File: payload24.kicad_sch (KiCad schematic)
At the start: 21 parts, among them J1 532540370, J2 532540370, J3 460150206, J4 532540370, Q1 CSD19503KCS, Q2 CSD19503KCS, SW1 FingerTech

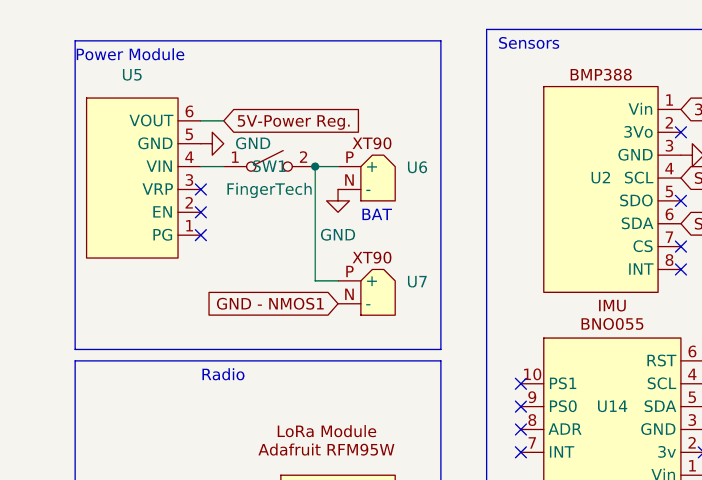
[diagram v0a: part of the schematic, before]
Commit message: PCB layer and power setup
Made PCB 6-Layers
Routed .1in power connection
Setup power plane thermal relief spoke width and gap
Moved Mosfet, power regular, and other components around a little
Rotated PCB 21 degrees
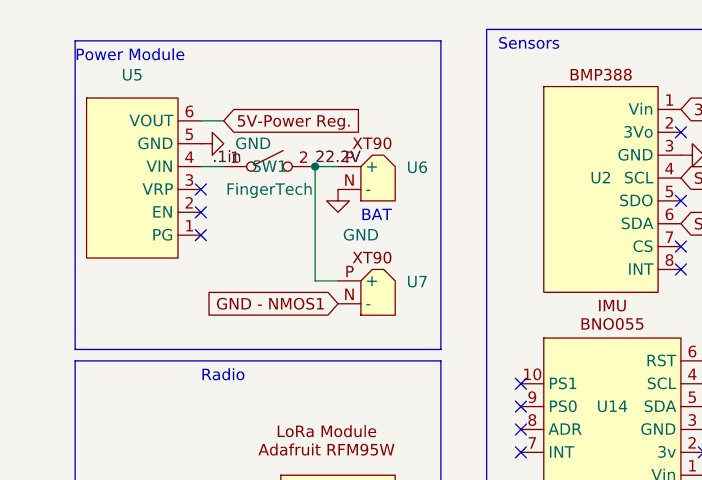
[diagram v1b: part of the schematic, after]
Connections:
- net 22.2V: now reaches SW1.2 (B), U6.P (+), U7.P (+)
- net .1in: now reaches SW1.1 (A), U5.4 (VIN)
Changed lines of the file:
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@@
+    (effects (font (size 1.27 1.27)) (justify left bottom))
+  )
+  (label "22.2V" (at 46.99 30.48 0) (fields_autoplaced)
+    (effects (font (size 1.27 1.27)) (justify left bottom))
+  )
+  (label ".1in" (at 35.56 30.48 0) (fields_autoplaced)
     (effects (font (size 1.27 1.27)) (justify left bottom))
   )
@@
   )
   (symbol (lib_id "power:GND") (at 49.53 33.02 0) (unit 1)
-    (in_bom yes) (on_board yes) (dnp no) (fields_autoplaced)
+    (in_bom yes) (on_board yes) (dnp no)
     (property "Reference" "#PWR018" (at 49.53 39.37 0)
       (effects (font (size 1.27 1.27)) hide)
     )
-    (property "Value" "GND" (at 49.53 38.1 0)
-      (effects (font (size 1.27 1.27)))
-    )
+    (property "Value" "GND" (at 52.07 38.1 0)
+      (effects (font (size 1.27 1.27)))
+    )

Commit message: final updates prior to purchasing (1/17)
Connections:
- net GND: now also Q2.3, R3.1
- net GND - NMOS1: no longer Q2.3, R3.1
- net Altitude Signal: no longer names the net of U1.29 (PWM|TX7)
- no-connect marks 53 -> 54
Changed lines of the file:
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@@
   (no_connect (at 58.42 87.63))
   (no_connect (at 90.17 92.71))
+  (no_connect (at 130.81 72.39))
   (no_connect (at 90.17 85.09))
   (no_connect (at 58.42 74.93))
@@
     )
   )
-  (global_label "GND - NMOS1" (shape input) (at 59.69 124.46 180) (fields_autoplaced)
-    (effects (font (size 1.27 1.27)) (justify right))
-    (property "Intersheetrefs" "${INTERSHEET_REFS}" (at 42.7953 124.46 0)
-      (effects (font (size 1.27 1.27)) (justify right) hide)
-    )
-  )
   (global_label "SCL1" (shape input) (at 87.63 110.49 0) (fields_autoplaced)
     (effects (font (size 1.27 1.27)) (justify left))
@@
     (effects (font (size 1.27 1.27)) (justify right))
     (property "Intersheetrefs" "${INTERSHEET_REFS}" (at 123.2286 54.61 0)
-      (effects (font (size 1.27 1.27)) (justify right) hide)
-    )
-  )
-  (global_label "Altitude Signal" (shape input) (at 130.81 72.39 180) (fields_autoplaced)
-    (effects (font (size 1.27 1.27)) (justify right))
-    (property "Intersheetrefs" "${INTERSHEET_REFS}" (at 113.7341 72.39 0)
       (effects (font (size 1.27 1.27)) (justify right) hide)
     )
@@
         )
       )
+    )
+  )
+  (symbol (lib_id "power:GND") (at 59.69 124.46 0) (unit 1)
+    (in_bom yes) (on_board yes) (dnp no)
+    (property "Reference" "#PWR02" (at 59.69 130.81 0)
+      (effects (font (size 1.27 1.27)) hide)
+    )
+    (property "Value" "GND" (at 59.69 127 90)
+      (effects (font (size 1.27 1.27)) (justify right))
+    )
+    (property "Footprint" "" (at 59.69 124.46 0)
+      (effects (font (size 1.27 1.27)) hide)
+    )
+    (property "Datasheet" "" (at 59.69 124.46 0)
+      (effects (font (size 1.27 1.27)) hide)
+    )
+    (pin "1")
+    (instances
+      (project "payload24"
+        (path "/2e97abcc-083d-4cb7-a03a-25669793abd8"
+          (reference "#PWR02") (unit 1)
+        )
+      )

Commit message: PCB laid out
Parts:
- removed J1, J2, J4: 532540370, JST-XH3:JST-XH3, symbol molexConnector:532540370
- removed J3: 460150206, JST-XH2:JST-XH2, symbol molex2pin:460150206
- removed Q1: CSD19503KCS, teensyMosfet:teensyMosfet, symbol teensyMosfet:CSD19503KCS
- removed R1: 500, 500Ohm:RESC3216X65N, symbol Device:R_US
- removed R4: 10K, 10KOhm:RESC3216X70N, symbol Device:R_US
- removed U13: ~, Trinket M0:Trinket M0, symbol Trinket M0:Trinket_M0
- removed U2: ~, BMP388:BMP388, symbol BMP388:BMP388
- removed U7: ~, XT60:AMASS_XT60-M, symbol PowerConnectors:XT90
- added J1: JST-XH3, JST-XH3:JST-XH3, symbol 532540370:JST-XH3
- added J2: PixHawk, JST-XH2:JST-XH2, symbol 532540370:JST-XH2
- added J3, J4: Motors, JST-XH3:JST-XH4, symbol 532540370:JST-XH4
- added Q3: IRLB4132, teensyMosfet:teensyMosfet, symbol Simulation_SPICE:NMOS
- added R5: 1000, 1kOhm:RESC3216X70N, symbol Device:R_US
- added R6: 10K, 10KOhm:RESC3216X70N, symbol Device:R_US
- added U2, U7: LMS1585ACT-3.3/NOPB, teensyMosfet:vRegulator, symbol Regulator_Linear:LD1117S33TR_SOT223
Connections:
- net GND - NMOS1 is gone; now on net GND: U1.GND1 (GND), U1.GND2 (GND), U1.GND3 (GND), U14.3 (GND), U3.3 (GND), U4.2 (GND), U8.3 (GND)
- net .1in: now also SW1.2 (B); no longer SW1.1 (A)
- net 22.2V: now also SW1.1 (A); no longer SW1.2 (B)
- net 5V-Power Reg.: now also J1.2 (+), J2.1 (+), U2.3 (VI), U7.3 (VI)
- net GND: now also J1.3 (-), Q3.3 (S), R6.2, U2.1 (GND), U7.1 (GND)
- net Open Signal: now also U1.27 (SCK1|A13), R5.1; no longer U1.14 (A0|TX3|S/PDIF_OUT|PWM)
- net PixHawk Signal: no longer U1.28 (PWM|RX7)
- net Retention  Signal: now also J1.1 (PWM)
- net GND - NMOS2: no longer names the net of Q2.2
- net GND - NMOS2: now also J2.2 (-)
- new net: J3.3 (-), J3.4 (-), J4.3 (-), J4.4 (-), Q3.1 (D)
- new net: Q3.2 (G), R5.2, R6.1
- new net: J4.1 (+), J4.2 (+), U7.2 (VO)
- new net: J3.1 (+), J3.2 (+), U2.2 (VO)
- no-connect marks 54 -> 47
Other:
- note removed: "PixHawk Power"
- note removed: "Power Mosfets"
- note removed: "Propellers & Landing Gear Servo"
- company: Anthony Konstantinidi and Kathleen Arrington -> (none)
- moved on the sheet: SW1, U1, U14, U3, U4, U5, U6, U8

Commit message: update
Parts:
- removed Q2: CSD19503KCS, teensyMosfet:teensyMosfet, symbol teensyMosfet:CSD19503KCS
- added C1, C2, C3: 10μF, CAPC3216X110N:CAPC3216X110N, symbol Device:C
- added Q1: IRLB4132, teensyMosfet:teensyMosfet, symbol Simulation_SPICE:NMOS
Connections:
- net 5V-Power Reg.: now also C3.1
- net GND: now also C1.2, C2.2, C3.2, Q1.3 (S)
- net at J2.2 (-): now also Q1.1 (D)
- net at J4.1 (+), J4.2 (+), U7.2 (VO): now also C2.1
- net at R2.2, R3.2: now also Q1.2 (G)
- net at J3.1 (+), J3.2 (+), U2.2 (VO): now also C1.1
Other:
- moved on the sheet: Q3, R5, R6, U2, U7

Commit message: updated payload
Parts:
- added LS1: PT-1241PFQ, buzzer_PT-1241PFQ:buzz_PT-1241PFQ_MAL, symbol buzzer_PT-1241PFQ:PT-1241PFQ
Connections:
- net GND: now also LS1.2
- net at U1.18 (A4|SDA|PWM): now also LS1.1
- net RST3: no longer names the net of U1.2 (PWM|OUT2)
- net RST3: no longer U4.9 (RST)
- no-connect marks 47 -> 48
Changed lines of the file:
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@@
   (junction (at 23.495 107.315) (diameter 0) (color 0 0 0 0)
   )
+  (junction (at 41.275 108.585) (diameter 0) (color 0 0 0 0)
+  )
+  (junction (at 19.05 94.615) (diameter 0) (color 0 0 0 0)
+  )
+  (junction (at 53.975 102.235) (diameter 0) (color 0 0 0 0)
+  )
+  (junction (at 41.275 94.615) (diameter 0) (color 0 0 0 0)
+  )
+  (junction (at 59.055 107.315) (diameter 0) (color 0 0 0 0)
+  )
+  (junction (at 50.165 125.73) (diameter 0) (color 0 0 0 0)
+  )
+  (junction (at 41.275 102.235) (diameter 0) (color 0 0 0 0)
+  )
   (junction (at 86.995 112.395) (diameter 0) (color 0 0 0 0)
-  )
-  (junction (at 41.275 108.585) (diameter 0) (color 0 0 0 0)
-  )
-  (junction (at 19.05 94.615) (diameter 0) (color 0 0 0 0)
-  )
-  (junction (at 53.975 102.235) (diameter 0) (color 0 0 0 0)
-  )
-  (junction (at 41.275 94.615) (diameter 0) (color 0 0 0 0)
-  )
-  (junction (at 59.055 107.315) (diameter 0) (color 0 0 0 0)
-  )
-  (junction (at 50.165 125.73) (diameter 0) (color 0 0 0 0)
-  )
-  (junction (at 41.275 102.235) (diameter 0) (color 0 0 0 0)
   )
   (no_connect (at 173.355 34.29))
@@
   (no_connect (at 128.905 77.47))
   (no_connect (at 128.905 64.77))
+  (no_connect (at 79.375 29.21))
   (no_connect (at 193.675 34.29))
   (no_connect (at 53.975 74.295))
   (no_connect (at 193.675 64.77))
+  (no_connect (at 36.195 74.295))
   (no_connect (at 79.375 72.39))
   (no_connect (at 193.675 57.15))
@@
   (no_connect (at 191.135 77.47))
   (no_connect (at 79.375 31.75))
-  (no_connect (at 128.905 41.91))
   (no_connect (at 53.975 53.975))
   (no_connect (at 79.375 64.77))
@@
     (stroke (width 0) (type default))
   )
+  (wire (pts (xy 94.615 99.695) (xy 94.615 107.315))
+    (stroke (width 0) (type default))
+  )
+  (wire (pts (xy 15.24 107.315) (xy 15.24 94.615))
+    (stroke (width 0) (type default))
+  )
+  (wire (pts (xy 94.615 117.475) (xy 94.615 125.095))
+    (stroke (width 0) (type default))
+  )
+  (wire (pts (xy 99.695 97.155) (xy 86.995 97.155))
+    (stroke (width 0) (type default))
+  )
   (wire (pts (xy 84.455 112.395) (xy 86.995 112.395))
     (stroke (width 0) (type default))
   )
-  (wire (pts (xy 15.24 107.315) (xy 15.24 94.615))
-    (stroke (width 0) (type default))
-  )
-  (wire (pts (xy 99.695 97.155) (xy 86.995 97.155))
-    (stroke (width 0) (type default))
-  )
   (wire (pts (xy 43.18 125.73) (xy 50.165 125.73))
     (stroke (width 0) (type default))
   )
+  (wire (pts (xy 86.995 112.395) (xy 86.995 114.935))
+    (stroke (width 0) (type default))
+  )
   (wire (pts (xy 15.24 94.615) (xy 19.05 94.615))
     (stroke (width 0) (type default))
@@
     (stroke (width 0) (type default))
   )
+  (wire (pts (xy 59.055 106.045) (xy 59.055 107.315))
+    (stroke (width 0) (type default))
+  )
+  (wire (pts (xy 28.575 102.235) (xy 41.275 102.235))
+    (stroke (width 0) (type default))
+  )
+  (wire (pts (xy 23.495 106.045) (xy 23.495 107.315))
+    (stroke (width 0) (type default))
+  )
+  (wire (pts (xy 42.545 27.94) (xy 45.085 27.94))
+    (stroke (width 0) (type default))
+  )
+  (wire (pts (xy 41.275 108.585) (xy 41.275 112.395))
+    (stroke (width 0) (type default))
+  )
+  (wire (pts (xy 128.905 41.91) (xy 146.685 41.91))
+    (stroke (width 0) (type default))
+  )
+  (wire (pts (xy 34.925 53.975) (xy 36.195 53.975))
+    (stroke (width 0) (type default))
+  )
+  (wire (pts (xy 59.055 107.315) (xy 67.31 107.315))
+    (stroke (width 0) (type default))
+  )
+  (wire (pts (xy 62.865 94.615) (xy 61.595 94.615))
+    (stroke (width 0) (type default))
+  )
+  (wire (pts (xy 19.05 94.615) (xy 20.955 94.615))
+    (stroke (width 0) (type default))
+  )
+  (wire (pts (xy 93.345 125.095) (xy 93.345 127.635))
+    (stroke (width 0) (type default))
+  )
+  (wire (pts (xy 41.275 94.615) (xy 46.355 94.615))
+    (stroke (width 0) (type default))
+  )
+  (wire (pts (xy 23.495 107.315) (xy 23.495 108.585))
+    (stroke (width 0) (type default))
+  )
+  (wire (pts (xy 74.295 112.395) (xy 76.835 112.395))
+    (stroke (width 0) (type default))
+  )
   (wire (pts (xy 86.995 99.695) (xy 94.615 99.695))
-    (stroke (width 0) (type default))
-  )
-  (wire (pts (xy 59.055 106.045) (xy 59.055 107.315))
-    (stroke (width 0) (type default))
-  )
-  (wire (pts (xy 28.575 102.235) (xy 41.275 102.235))
-    (stroke (width 0) (type default))
-  )
-  (wire (pts (xy 94.615 117.475) (xy 94.615 125.095))
-    (stroke (width 0) (type default))
-  )
-  (wire (pts (xy 23.495 106.045) (xy 23.495 107.315))
-    (stroke (width 0) (type default))
-  )
-  (wire (pts (xy 42.545 27.94) (xy 45.085 27.94))
-    (stroke (width 0) (type default))
-  )
-  (wire (pts (xy 41.275 108.585) (xy 41.275 112.395))
-    (stroke (width 0) (type default))
-  )
-  (wire (pts (xy 94.615 99.695) (xy 94.615 107.315))
-    (stroke (width 0) (type default))
-  )
-  (wire (pts (xy 86.995 112.395) (xy 86.995 114.935))
-    (stroke (width 0) (type default))
-  )
-  (wire (pts (xy 34.925 53.975) (xy 36.195 53.975))
-    (stroke (width 0) (type default))
-  )
-  (wire (pts (xy 59.055 107.315) (xy 67.31 107.315))
-    (stroke (width 0) (type default))
-  )
-  (wire (pts (xy 62.865 94.615) (xy 61.595 94.615))
-    (stroke (width 0) (type default))
-  )
-  (wire (pts (xy 19.05 94.615) (xy 20.955 94.615))
-    (stroke (width 0) (type default))
-  )
-  (wire (pts (xy 93.345 125.095) (xy 93.345 127.635))
-    (stroke (width 0) (type default))
-  )
-  (wire (pts (xy 41.275 94.615) (xy 46.355 94.615))
-    (stroke (width 0) (type default))
-  )
-  (wire (pts (xy 23.495 107.315) (xy 23.495 108.585))
-    (stroke (width 0) (type default))
-  )
-  (wire (pts (xy 74.295 112.395) (xy 76.835 112.395))
     (stroke (width 0) (type default))
   )
@@
     )
   )
-  (global_label "RST3" (shape input) (at 79.375 29.21 180) (fields_autoplaced)
-    (effects (font (size 1.27 1.27)) (justify right))
-    (property "Intersheetrefs" "${INTERSHEET_REFS}" (at 71.7332 29.21 0)
-      (effects (font (size 1.27 1.27)) (justify right) hide)
-    )
-  )
   (global_label "G0" (shape input) (at 79.375 74.93 180) (fields_autoplaced)
     (effects (font (size 1.27 1.27)) (justify right))
@@
     (property "Intersheetrefs" "${INTERSHEET_REFS}" (at 136.6073 46.99 0)
       (effects (font (size 1.27 1.27)) (justify left) hide)
-    )
-  )
-  (global_label "RST3" (shape input) (at 36.195 74.295 180) (fields_autoplaced)
-    (effects (font (size 1.27 1.27)) (justify right))
-    (property "Intersheetrefs" "${INTERSHEET_REFS}" (at 28.5532 74.295 0)
-      (effects (font (size 1.27 1.27)) (justify right) hide)
     )
   )
@@
         (path "/2e97abcc-083d-4cb7-a03a-25669793abd8"
           (reference "#PWR011") (unit 1)
+        )
+      )
+    )
+  )
+  (symbol (lib_id "power:GND") (at 146.685 44.45 270) (unit 1)
+    (in_bom yes) (on_board yes) (dnp no)
+    (property "Reference" "#PWR05" (at 140.335 44.45 0)
+      (effects (font (size 1.27 1.27)) hide)
+    )
+    (property "Value" "GND" (at 143.51 44.45 90)
+      (effects (font (size 1.27 1.27)) (justify right))
+    )
+    (property "Footprint" "" (at 146.685 44.45 0)
+      (effects (font (size 1.27 1.27)) hide)
+    )
+    (property "Datasheet" "" (at 146.685 44.45 0)
+      (effects (font (size 1.27 1.27)) hide)
+    )
+    (pin "1")
+    (instances
+      (project "payload24"
+        (path "/2e97abcc-083d-4cb7-a03a-25669793abd8"
+          (reference "#PWR05") (unit 1)
         )
       )
@@
     )
   )
+  (symbol (lib_id "buzzer_PT-1241PFQ:PT-1241PFQ") (at 146.685 41.91 0) (unit 1)
+    (in_bom yes) (on_board yes) (dnp no) (fields_autoplaced)
+    (property "Reference" "LS1" (at 160.02 41.91 0)
+      (effects (font (size 1.524 1.524)) (justify left))
+    )
+    (property "Value" "PT-1241PFQ" (at 160.02 44.45 0)
+      (effects (font (size 1.524 1.524)) (justify left))
+    )
+    (property "Footprint" "buzzer_PT-1241PFQ:buzz_PT-1241PFQ_MAL" (at 146.685 41.91 0)
+      (effects (font (size 1.27 1.27) italic) hide)
+    )
+    (property "Datasheet" "PT-1241PFQ" (at 146.685 41.91 0)
+      (effects (font (size 1.27 1.27) italic) hide)
+    )
+    (pin "1")
+    (pin "2")
+    (instances
+      (project "payload24"
+        (path "/2e97abcc-083d-4cb7-a03a-25669793abd8"
+          (reference "LS1") (unit 1)
+        )
+      )
+    )
+  )
   (symbol (lib_id "Simulation_SPICE:NMOS") (at 92.075 112.395 0) (unit 1)
     (in_bom yes) (on_board yes) (dnp no)
@@
       (effects (font (size 1.27 1.27)) hide)
     )
-    (property "Value" "GND" (at 145.415 34.29 90)
+    (property "Value" "GND" (at 144.78 34.29 90)
       (effects (font (size 1.27 1.27)) (justify right))
     )

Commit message: UPDATeEE
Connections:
- net PixHawk Signal: now also U1.28 (PWM|RX7)
- net SCL2: now also U14.5 (SCL); no longer U14.4 (SCL)
- net SDA2: now also U14.4 (SDA); no longer U14.5 (SDA)
- no-connect marks 48 -> 47
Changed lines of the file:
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@@
   (no_connect (at 191.135 90.17))
   (no_connect (at 191.135 85.09))
-  (no_connect (at 79.375 69.85))
   (no_connect (at 128.905 52.07))
   (no_connect (at 79.375 36.83))
@@
     )
   )
+  (global_label "PixHawk Signal" (shape input) (at 79.375 69.85 180) (fields_autoplaced)
+    (effects (font (size 1.27 1.27)) (justify right))
+    (property "Intersheetrefs" "${INTERSHEET_REFS}" (at 61.7547 69.85 0)
+      (effects (font (size 1.27 1.27)) (justify right) hide)
+    )
+  )

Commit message: update
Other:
- company: (none) -> Anthony Konstantinidi
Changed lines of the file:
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@@
     (date "2024-01-06")
     (rev "3")
+    (company "Anthony Konstantinidi")
   )
   (junction (at 43.18 117.475) (diameter 0) (color 0 0 0 0)
